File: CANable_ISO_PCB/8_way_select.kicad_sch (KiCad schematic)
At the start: 8 parts

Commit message: CANchovy Rev A release.
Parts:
- JP1, JP2, JP3, JP4, JP5: now left out of the parts list
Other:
- company: (none) -> N/A
- title: (none) -> 8-Way Select
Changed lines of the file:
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@@
 (kicad_sch (version 20230121) (generator eeschema)
   (paper "A4")
+  (title_block
+    (title "8-Way Select")
+    (date "2023-10-31")
+    (rev "A")
+    (company "N/A")
+    (comment 1 "MKS CANable V2 based")
+  )
   (junction (at 160.02 93.98) (diameter 0) (color 0 0 0 0)
   )
@@
   )
   (symbol (lib_id "Jumper:SolderJumper_2_Open") (at 142.24 77.47 0) (unit 1)
-    (in_bom yes) (on_board yes) (dnp no)
+    (in_bom no) (on_board yes) (dnp no)
     (property "Reference" "JP4" (at 137.16 76.2 0)
       (effects (font (size 1.27 1.27)))
@@
       (effects (font (size 1.27 1.27)) hide)
     )
+    (property "Manufacturer" "" (at 142.24 77.47 0)
+      (effects (font (size 1.27 1.27)) hide)
+    )
+    (property "Manufacturer Part #" "" (at 142.24 77.47 0)
+      (effects (font (size 1.27 1.27)) hide)
+    )
+    (property "LCSC Part #" "" (at 142.24 77.47 0)
+      (effects (font (size 1.27 1.27)) hide)
+    )
     (pin "1")
     (pin "2")
@@
   )
   (symbol (lib_id "Jumper:SolderJumper_2_Open") (at 142.24 101.6 0) (unit 1)
-    (in_bom yes) (on_board yes) (dnp no)
+    (in_bom no) (on_board yes) (dnp no)
     (property "Reference" "JP1" (at 137.16 100.33 0)
       (effects (font (size 1.27 1.27)))
@@
       (effects (font (size 1.27 1.27)) hide)
     )
+    (property "Manufacturer" "" (at 142.24 101.6 0)
+      (effects (font (size 1.27 1.27)) hide)
+    )
+    (property "Manufacturer Part #" "" (at 142.24 101.6 0)
+      (effects (font (size 1.27 1.27)) hide)
+    )
+    (property "LCSC Part #" "" (at 142.24 101.6 0)
+      (effects (font (size 1.27 1.27)) hide)
+    )
     (pin "1")
     (pin "2")
@@
   )
   (symbol (lib_id "Jumper:SolderJumper_2_Open") (at 142.24 93.98 0) (unit 1)
-    (in_bom yes) (on_board yes) (dnp no)
+    (in_bom no) (on_board yes) (dnp no)
     (property "Reference" "JP2" (at 137.16 92.71 0)
       (effects (font (size 1.27 1.27)))
@@
       (effects (font (size 1.27 1.27)) hide)
     )
+    (property "Manufacturer" "" (at 142.24 93.98 0)
+      (effects (font (size 1.27 1.27)) hide)
+    )
+    (property "Manufacturer Part #" "" (at 142.24 93.98 0)
+      (effects (font (size 1.27 1.27)) hide)
+    )
+    (property "LCSC Part #" "" (at 142.24 93.98 0)
+      (effects (font (size 1.27 1.27)) hide)
+    )
     (pin "1")
     (pin "2")
@@
   )
   (symbol (lib_id "Jumper:SolderJumper_2_Open") (at 142.24 116.84 0) (unit 1)
-    (in_bom yes) (on_board yes) (dnp no)
+    (in_bom no) (on_board yes) (dnp no)
     (property "Reference" "JP1" (at 137.16 115.57 0)
       (effects (font (size 1.27 1.27)))
@@
       (effects (font (size 1.27 1.27)) hide)
     )
+    (property "Manufacturer" "" (at 142.24 116.84 0)
+      (effects (font (size 1.27 1.27)) hide)
+    )
+    (property "Manufacturer Part #" "" (at 142.24 116.84 0)
+      (effects (font (size 1.27 1.27)) hide)
+    )
+    (property "LCSC Part #" "" (at 142.24 116.84 0)
+      (effects (font (size 1.27 1.27)) hide)
+    )
     (pin "1")
     (pin "2")
@@
   )
   (symbol (lib_id "Jumper:SolderJumper_2_Open") (at 142.24 69.85 0) (unit 1)
-    (in_bom yes) (on_board yes) (dnp no)
+    (in_bom no) (on_board yes) (dnp no)
     (property "Reference" "JP5" (at 137.16 68.58 0)
       (effects (font (size 1.27 1.27)))
@@
       (effects (font (size 1.27 1.27)) hide)
     )
+    (property "Manufacturer" "" (at 142.24 69.85 0)
+      (effects (font (size 1.27 1.27)) hide)
+    )
+    (property "Manufacturer Part #" "" (at 142.24 69.85 0)
+      (effects (font (size 1.27 1.27)) hide)
+    )
+    (property "LCSC Part #" "" (at 142.24 69.85 0)
+      (effects (font (size 1.27 1.27)) hide)
+    )
     (pin "1")
     (pin "2")
@@
   )
   (symbol (lib_id "Jumper:SolderJumper_2_Open") (at 142.24 86.36 0) (unit 1)
-    (in_bom yes) (on_board yes) (dnp no)
+    (in_bom no) (on_board yes) (dnp no)
     (property "Reference" "JP3" (at 137.16 85.09 0)
       (effects (font (size 1.27 1.27)))
@@
       (effects (font (size 1.27 1.27)) hide)
     )
+    (property "Manufacturer" "" (at 142.24 86.36 0)
+      (effects (font (size 1.27 1.27)) hide)
+    )
+    (property "Manufacturer Part #" "" (at 142.24 86.36 0)
+      (effects (font (size 1.27 1.27)) hide)
+    )
+    (property "LCSC Part #" "" (at 142.24 86.36 0)
+      (effects (font (size 1.27 1.27)) hide)
+    )
     (pin "1")
     (pin "2")
@@
   )
   (symbol (lib_id "Jumper:SolderJumper_2_Open") (at 142.24 124.46 0) (unit 1)
-    (in_bom yes) (on_board yes) (dnp no)
+    (in_bom no) (on_board yes) (dnp no)
     (property "Reference" "JP1" (at 137.16 123.19 0)
       (effects (font (size 1.27 1.27)))
@@
       (effects (font (size 1.27 1.27)) hide)
     )
+    (property "Manufacturer" "" (at 142.24 124.46 0)
+      (effects (font (size 1.27 1.27)) hide)
+    )
+    (property "Manufacturer Part #" "" (at 142.24 124.46 0)
+      (effects (font (size 1.27 1.27)) hide)
+    )
+    (property "LCSC Part #" "" (at 142.24 124.46 0)
+      (effects (font (size 1.27 1.27)) hide)
+    )
     (pin "1")
     (pin "2")
@@
   )
   (symbol (lib_id "Jumper:SolderJumper_2_Open") (at 142.24 109.22 0) (unit 1)
-    (in_bom yes) (on_board yes) (dnp no)
+    (in_bom no) (on_board yes) (dnp no)
     (property "Reference" "JP1" (at 137.16 107.95 0)
       (effects (font (size 1.27 1.27)))
@@
       (effects (font (size 1.27 1.27)) hide)
     )
+    (property "Manufacturer" "" (at 142.24 109.22 0)
+      (effects (font (size 1.27 1.27)) hide)
+    )
+    (property "Manufacturer Part #" "" (at 142.24 109.22 0)
+      (effects (font (size 1.27 1.27)) hide)
+    )
+    (property "LCSC Part #" "" (at 142.24 109.22 0)
+      (effects (font (size 1.27 1.27)) hide)
+    )

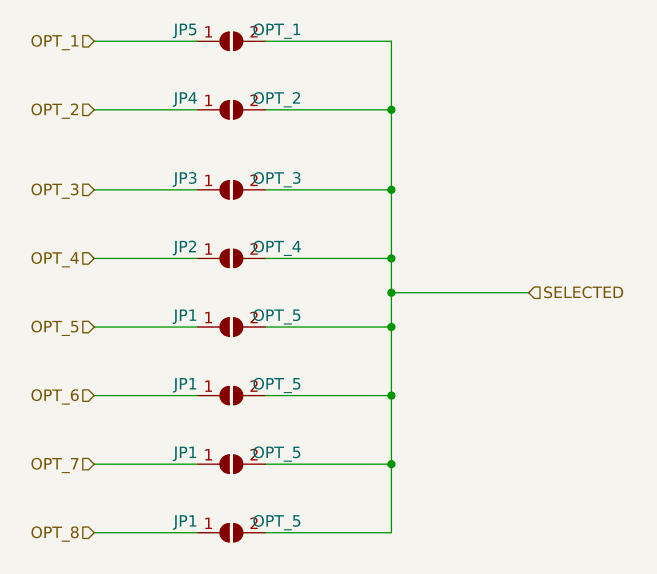
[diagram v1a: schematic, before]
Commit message: Corrected RJ45 footprint pinout and updated PCB to correctly label solder jumpers.
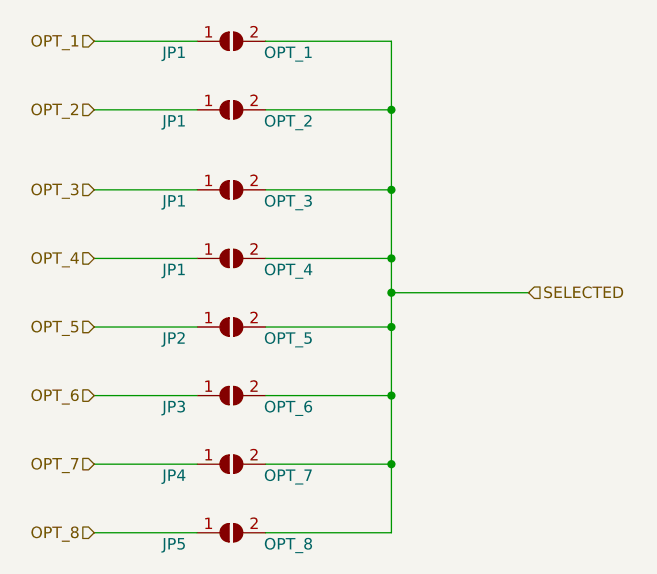
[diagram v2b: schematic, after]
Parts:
- JP1: value OPT_5 -> OPT_4
- JP1: value OPT_5 -> OPT_2
- JP1: value OPT_5 -> OPT_1
- JP1: value OPT_5 -> OPT_3
- JP2: value OPT_4 -> OPT_5
- JP3: value OPT_3 -> OPT_6
- JP4: value OPT_2 -> OPT_7
- JP5: value OPT_1 -> OPT_8
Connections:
- net OPT_1: now also JP1.1 (A); no longer JP5.1 (A)
- net OPT_2: now also JP1.1 (A); no longer JP4.1 (A)
- net OPT_3: now also JP1.1 (A); no longer JP3.1 (A)
- net OPT_4: now also JP1.1 (A); no longer JP2.1 (A)
- net OPT_5: now also JP2.1 (A); no longer JP1.1 (A)
- net OPT_6: now also JP3.1 (A); no longer JP1.1 (A)
- net OPT_7: now also JP4.1 (A); no longer JP1.1 (A)
- net OPT_8: now also JP5.1 (A); no longer JP1.1 (A)
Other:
- moved on the sheet: JP1, JP2, JP3, JP4, JP5
